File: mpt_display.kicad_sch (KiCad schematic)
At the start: 5 parts, among them J2 ER-TFT2.79-1, Q1 BSS138

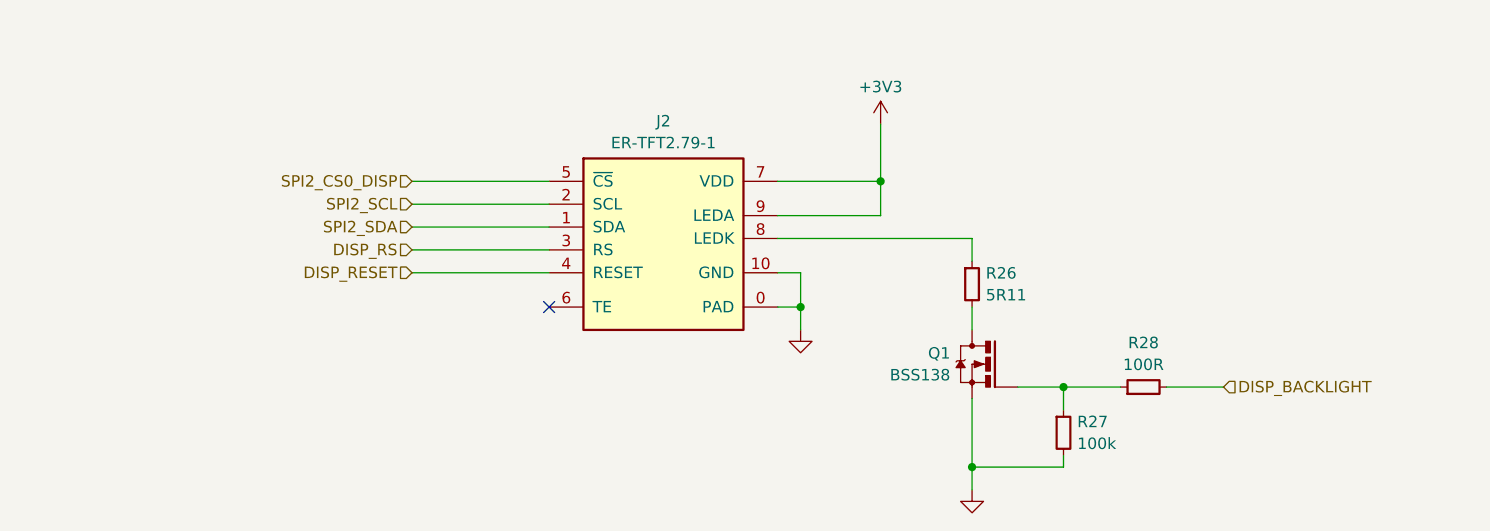
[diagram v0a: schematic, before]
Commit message: Added Info-Table for STAT Pins and LEDS of Charger Work In Progress regulation for Display driving (currently not working)
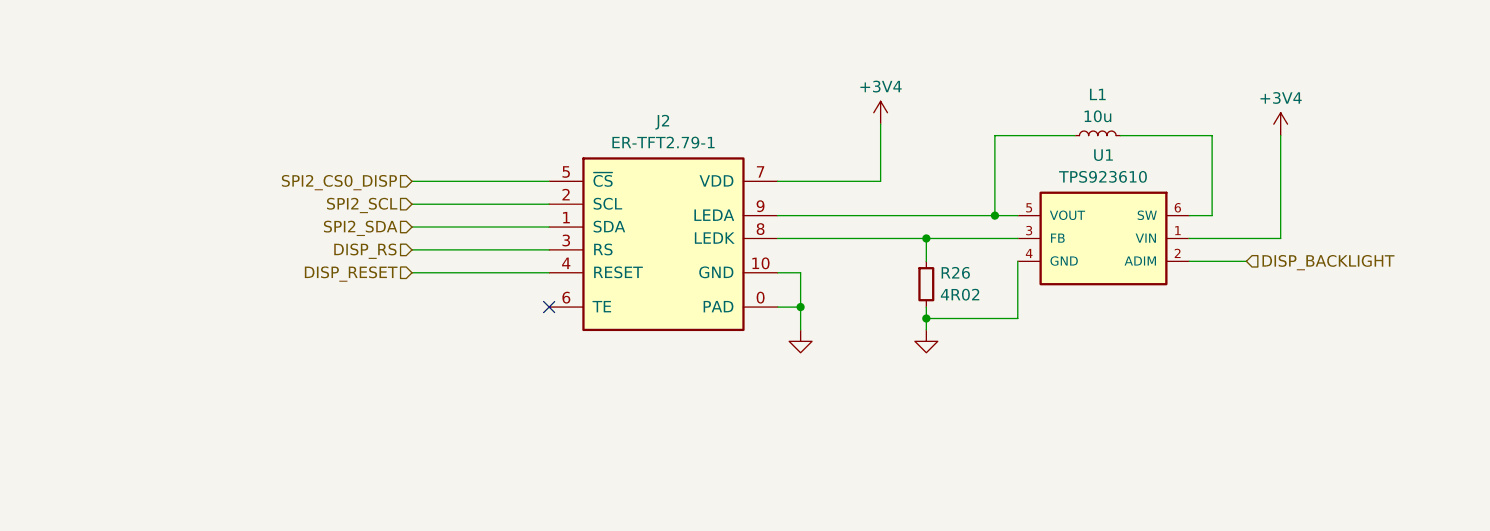
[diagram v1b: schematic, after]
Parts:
- removed Q1: BSS138, package:SOT-23, symbol db:mosfet/03.011.0000.0001
- removed R26: 5R11, passive:R_0805, symbol db:resistor_0805/00.018.0009.0037
- removed R27: 100k, passive:R_0603, symbol db:resistor_0603/00.018.0009.0047
- removed R28: 100R, passive:R_0603, symbol db:resistor_0603/00.018.0009.0044
- added L1: 10u, passive:L_0805, symbol db:inductor/02.046.0053.0001
- added R26: 4R02, passive:R_0603, symbol db:resistor_0603/00.018.0009.0448
- added U1: TPS923610, package:SOT-563, symbol db:ic/07.015.0044.0002
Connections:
- net DISP_BACKLIGHT: now also U1.2 (ADIM)
- net GND: now also R26.2, U1.4 (GND), U1.7 (PAD)
- net at J2.8 (LEDK): now also R26.1, U1.3 (FB)
- net +3V3: no longer names the net of J2.9 (LEDA)
- net +3V3: now also L1.1, U1.5 (VOUT); no longer J2.7 (VDD)
- new net: L1.2, U1.6 (SW)
- new net +3V4: J2.7 (VDD), U1.1 (VIN)

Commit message: Changed LED Driver for one with lower Headroom
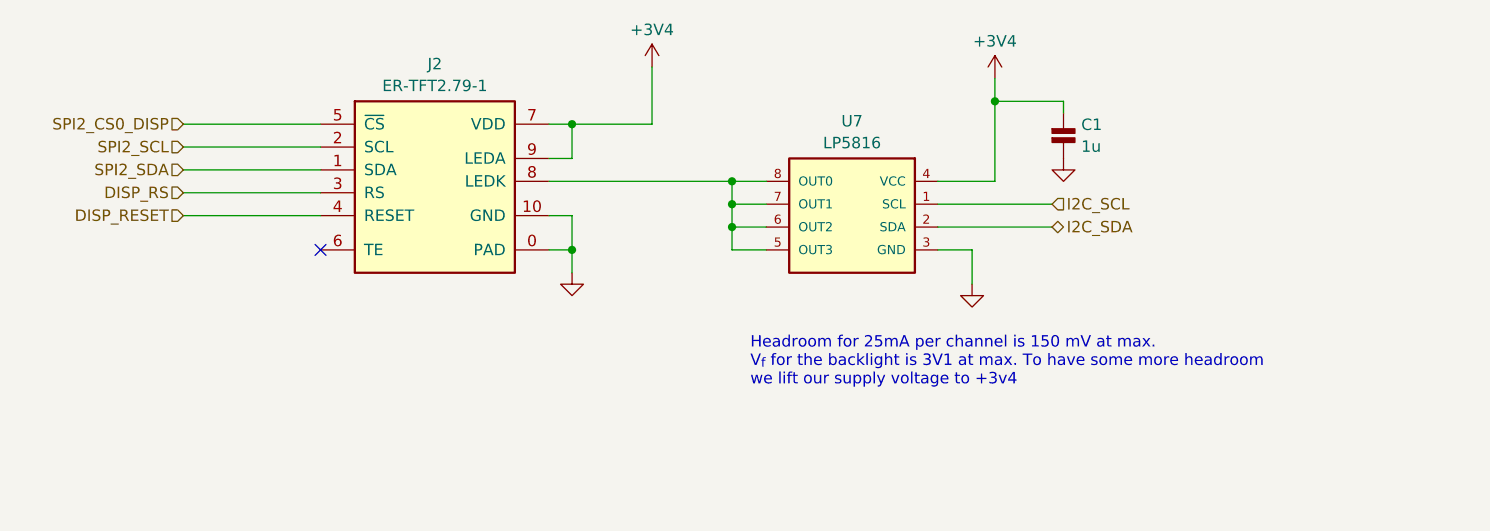
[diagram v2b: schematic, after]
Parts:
- removed L1: 10u, passive:L_0805, symbol db:inductor/02.046.0053.0001
- removed R26: 4R02, passive:R_0603, symbol db:resistor_0603/00.018.0009.0448
- removed U1: TPS923610, package:SOT-563, symbol db:ic/07.015.0044.0002
- added C1: 1u, passive:C_0603, symbol db:capacitor/01.018.0025.0013
- added U7: LP5816, package:SOT-583, symbol db:power_ic/11.015.0054.0001
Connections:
- net +3V4: now also J2.9 (LEDA), C1.1, U7.4 (VCC)
- net GND: now also C1.2, U7.3 (GND)
- net at J2.8 (LEDK): now also U7.5 (OUT3), U7.6 (OUT2), U7.7 (OUT1), U7.8 (OUT0)
- new net I2C_SCL: U7.1 (SCL)
- new net I2C_SDA: U7.2 (SDA)
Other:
- note added: "Headroom for 25mA per channel is 150 mV at max. V_{f} for the backlight is 3V1 at max. To have some more headroom we lift our supply voltage to +3v4"
- moved on the sheet: J2

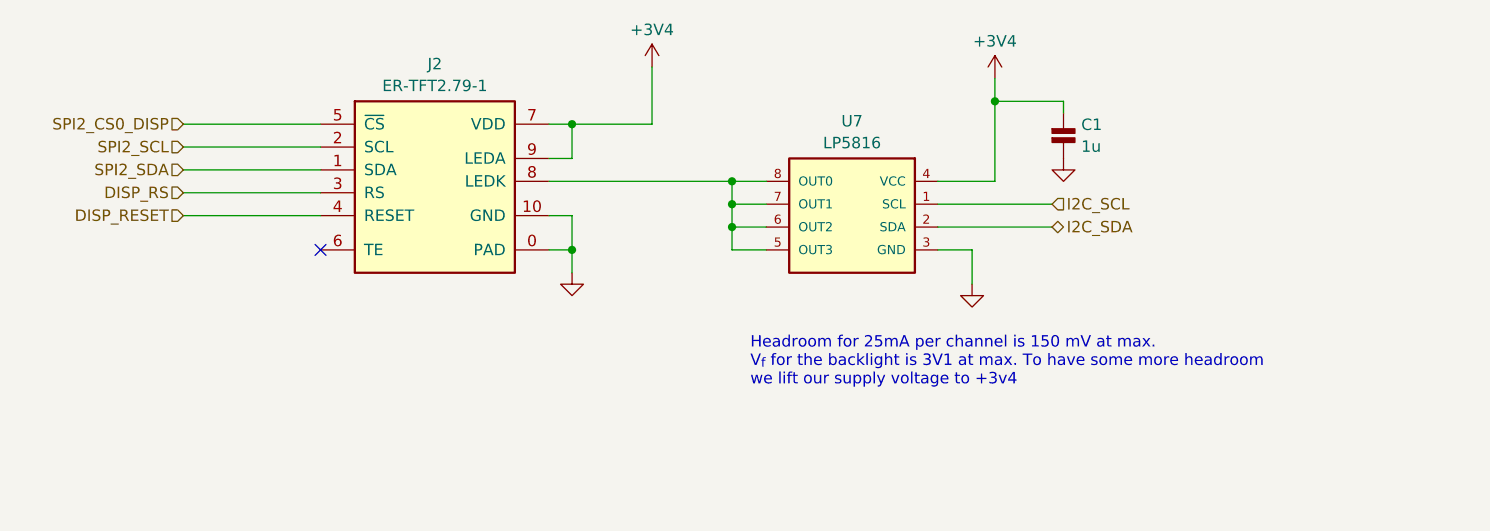
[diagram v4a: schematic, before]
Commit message: Replace LED Driver Remove maybe buzzer
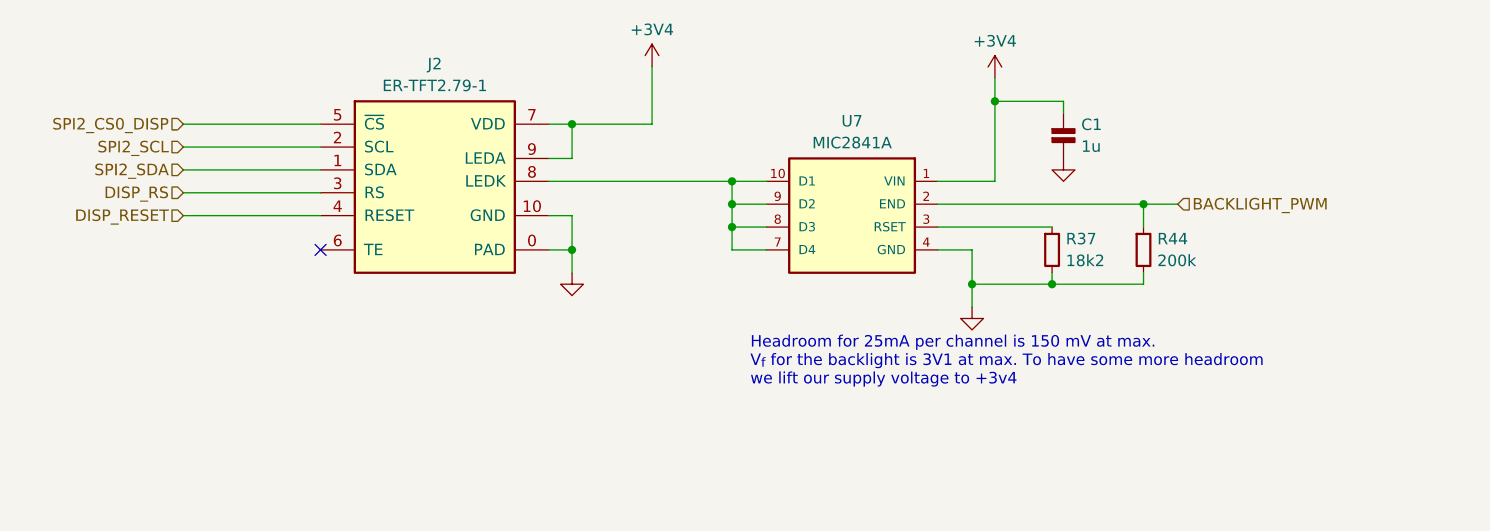
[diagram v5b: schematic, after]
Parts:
- added R37: 18k2, passive:R_0603, symbol db:resistor_0603/00.018.0009.0222
- added R44: 200k, passive:R_0603, symbol db:resistor_0603/00.018.0009.0251
- U7: value LP5816 -> MIC2841A; footprint package:SOT-583 -> package:MLF-10_MT_MCH; symbol db:power_ic/11.015.0054.0001 -> db:power_ic/11.047.0055.0001; Dist1# 296-LP5816DRLRCT-ND -> 576-3471-1-ND; FP SOT-583 -> MLF-10_MT_MCH; MFR TI -> Microchip; MFR# LP5816DRLR -> MIC2841AYMT-TR; Modified 2026-10-12 07:02:40 -> 2026-10-20 14:50:14; Rating 51mA per LED 4 Channel -> 20mA 4 Ch; Series LP -> MIC
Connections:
- net I2C_SCL is gone; now on net +3V4: U7.1 (VIN)
- net +3V4: no longer U7.4 (VCC)
- net GND: now also U7.0 (PAD), U7.4 (GND), R37.2, R44.2; no longer U7.3 (GND)
- net at J2.8 (LEDK), U7.7 (D4), U7.8 (D3): now also U7.10 (D1), U7.9 (D2); no longer U7.5 (OUT3), U7.6 (OUT2)
- net I2C_SDA renamed BACKLIGHT_PWM
- net BACKLIGHT_PWM: now also R44.1
- new net: R37.1, U7.3 (RSET)
